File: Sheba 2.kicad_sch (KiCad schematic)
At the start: 66 parts, among them J2 Conn_01x03_Pin, J3 Conn_01x03_Pin, J4 Conn_01x03_Pin, J7 Conn_01x06_Pin, J8 Conn_01x02_Pin, J9 Conn_02x04_Top_Bottom, P1 USB_C_Plug_USB2.0, SW1 SW_SPDT, U1 AP62300TWU, U3 MIC5504-3.3YM5, U4 STM32F072CBTx

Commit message: Actually get ready to add protections
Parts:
- removed Battery1: XT-60, Connector_AMASS:AMASS_XT60-F_1x02_P7.20mm_Vertical, symbol Device:Battery
- removed C1, C15: C0.1uF, Capacitor_SMD:C_1206_3216Metric_Pad1.33x1.80mm_HandSolder, symbol Device:C_Small
- removed C10, C12, C16, C18, C3, C5, C6, C7: C1uF, Capacitor_SMD:C_1206_3216Metric_Pad1.33x1.80mm_HandSolder, symbol Device:C_Small
- removed C11: C2.2uF, Capacitor_SMD:C_1206_3216Metric_Pad1.33x1.80mm_HandSolder, symbol Device:C_Small
- removed C13, C19: C22uF, Capacitor_SMD:C_1206_3216Metric_Pad1.33x1.80mm_HandSolder, symbol Device:C_Small
- removed C8: C10uF, Capacitor_SMD:C_1206_3216Metric_Pad1.33x1.80mm_HandSolder, symbol Device:C_Small
- removed C9: C0.01uF, Capacitor_SMD:C_1206_3216Metric_Pad1.33x1.80mm_HandSolder, symbol Device:C_Small
- removed D2, D4, D6, D7, D8: LED Green, LED_SMD:LED_1206_3216Metric_Pad1.42x1.75mm_HandSolder, symbol Device:LED
- removed D3, D5: LED Red, LED_SMD:LED_1206_3216Metric_Pad1.42x1.75mm_HandSolder, symbol Device:LED
- removed H1, H2, H3, H4: MountingHole_Pad, MountingHole:MountingHole_2.2mm_M2_DIN965_Pad, symbol Mechanical:MountingHole_Pad
- removed J2, J3, J4: Conn_01x03_Pin, Connector_PinSocket_2.54mm:PinSocket_1x03_P2.54mm_Vertical, symbol Connector:Conn_01x03_Pin
- removed L1: L3.3uH, Inductor_SMD:L_1206_3216Metric, symbol Device:L
- removed MD1, MD2, MD3: ZXBM5210-S, Package_SO:SOIC-8_3.9x4.9mm_P1.27mm, symbol Driver_Motor:ZXBM5210-S
- removed MT1: ICM-42670-P, Library:XDCR_ICM-42670-P, symbol ICM-42670-P:ICM-42670-P
- removed Motor Terminal1: 6x Motor Port, TerminalBlock_4Ucon:TerminalBlock_4Ucon_1x06_P3.50mm_Horizontal, symbol Connector:Screw_Terminal_01x06
- removed R10, R11, R12, R13, R6, R7, R8, R9: R220, Resistor_SMD:R_1206_3216Metric_Pad1.30x1.75mm_HandSolder, symbol Device:R
- removed R2, R4, R5: R10k, Resistor_SMD:R_1206_3216Metric_Pad1.30x1.75mm_HandSolder, symbol Device:R
- removed U1: AP62300TWU, Package_TO_SOT_SMD:TSOT-23-6_HandSoldering, symbol Regulator_Switching:AP62300TWU
- removed U3: MIC5504-3.3YM5, Package_TO_SOT_SMD:SOT-23-5_HandSoldering, symbol Regulator_Linear:MIC5504-3.3YM5
- D1: value LED Red -> LED Green; DigiKey 150120RS75000 -> 150120VS75000
- J1: renamed from J8; footprint Connector_PinHeader_2.54mm:PinHeader_1x02_P2.54mm_Vertical -> Connector_PinHeader_2.54mm:PinHeader_1x03_P2.54mm_Vertical; symbol Connector:Conn_01x02_Pin -> Connector:Conn_01x03_Pin
- R3: value R56.2k -> R220; DigiKey CRCW120652K3FKEA -> RMCF1206JT220R
- renumbered C2 to C1, C4 to C2, C14 to C3, C17 to C4, EP3 to EP1, EP1 to EP2, EP2 to EP3, J9 to J2, J7 to J3, R14 to R1, R1 to R2, U4 to U1
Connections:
- net +5V: no longer R3.1
- net BLINKY: now also R3.1
- net GND: now also D1.1 (K), J1.1 (Pin_1)
- net M3_REV: no longer D1.2 (A)
- net USART3_TX: now also J1.3 (Pin_3); no longer J1.1 (Pin_1)
- net at R3.2: now also D1.2 (A)
- net I2C2_SCL: no longer names the net of U1.26 (PB13)
- net I2C2_SDA: no longer names the net of U1.27 (PB14)
- net IMU_INT: no longer names the net of U1.28 (PB15)
- no-connect marks 12 -> 9
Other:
- added sheet Power & Motors (Power & Motors.kicad_sch)
- note added: "CPU STATUS LED"
- note added: "Kiwi/Differential Drive Switch"
- note removed: "12V to 5V"
- note removed: "3V3 LDO Power Supply"
- note removed: "AP_CS wired to VDD for I2C mode"
- note removed: "I2C Pull-ups"
- note removed: "IMU - Accel/Gyro/Temp chip ICM-42670-P"
- note removed: "Indicator LEDs"
- note removed: "Motor Controllers"
- note removed: "Servo Ports"
- note removed: "VIN: 4.2 to 18V"
- note removed: "VREF is wired to VDD to enable PWM control"
- moved on the sheet: C1, C2, C3, C4, EP1, EP2, EP3, J2, J3, P1, R1, R2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

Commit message: Ready to finalize Rev3
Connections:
- net GPIO0: now also U1.4 (PC15); no longer U1.42 (PB6)
- net GPIO5: now also U1.42 (PB6); no longer U1.4 (PC15)

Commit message: Rev3 ready to order
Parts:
- P1: value USB_C_Plug_USB2.0 -> USB 2.0 Type-C Port
- SW1: value SW_SPDT -> SPDT Switch
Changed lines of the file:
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@@
 			)
 		)
-		(property "Value" "USB_C_Plug_USB2.0"
+		(property "Value" "USB 2.0 Type-C Port"
 			(at 161.29 71.12 0)
 			(effects
@@
 			)
 		)
-		(property "Value" "SW_SPDT"
+		(property "Value" "SPDT Switch"
 			(at 105.41 95.25 0)
 			(effects

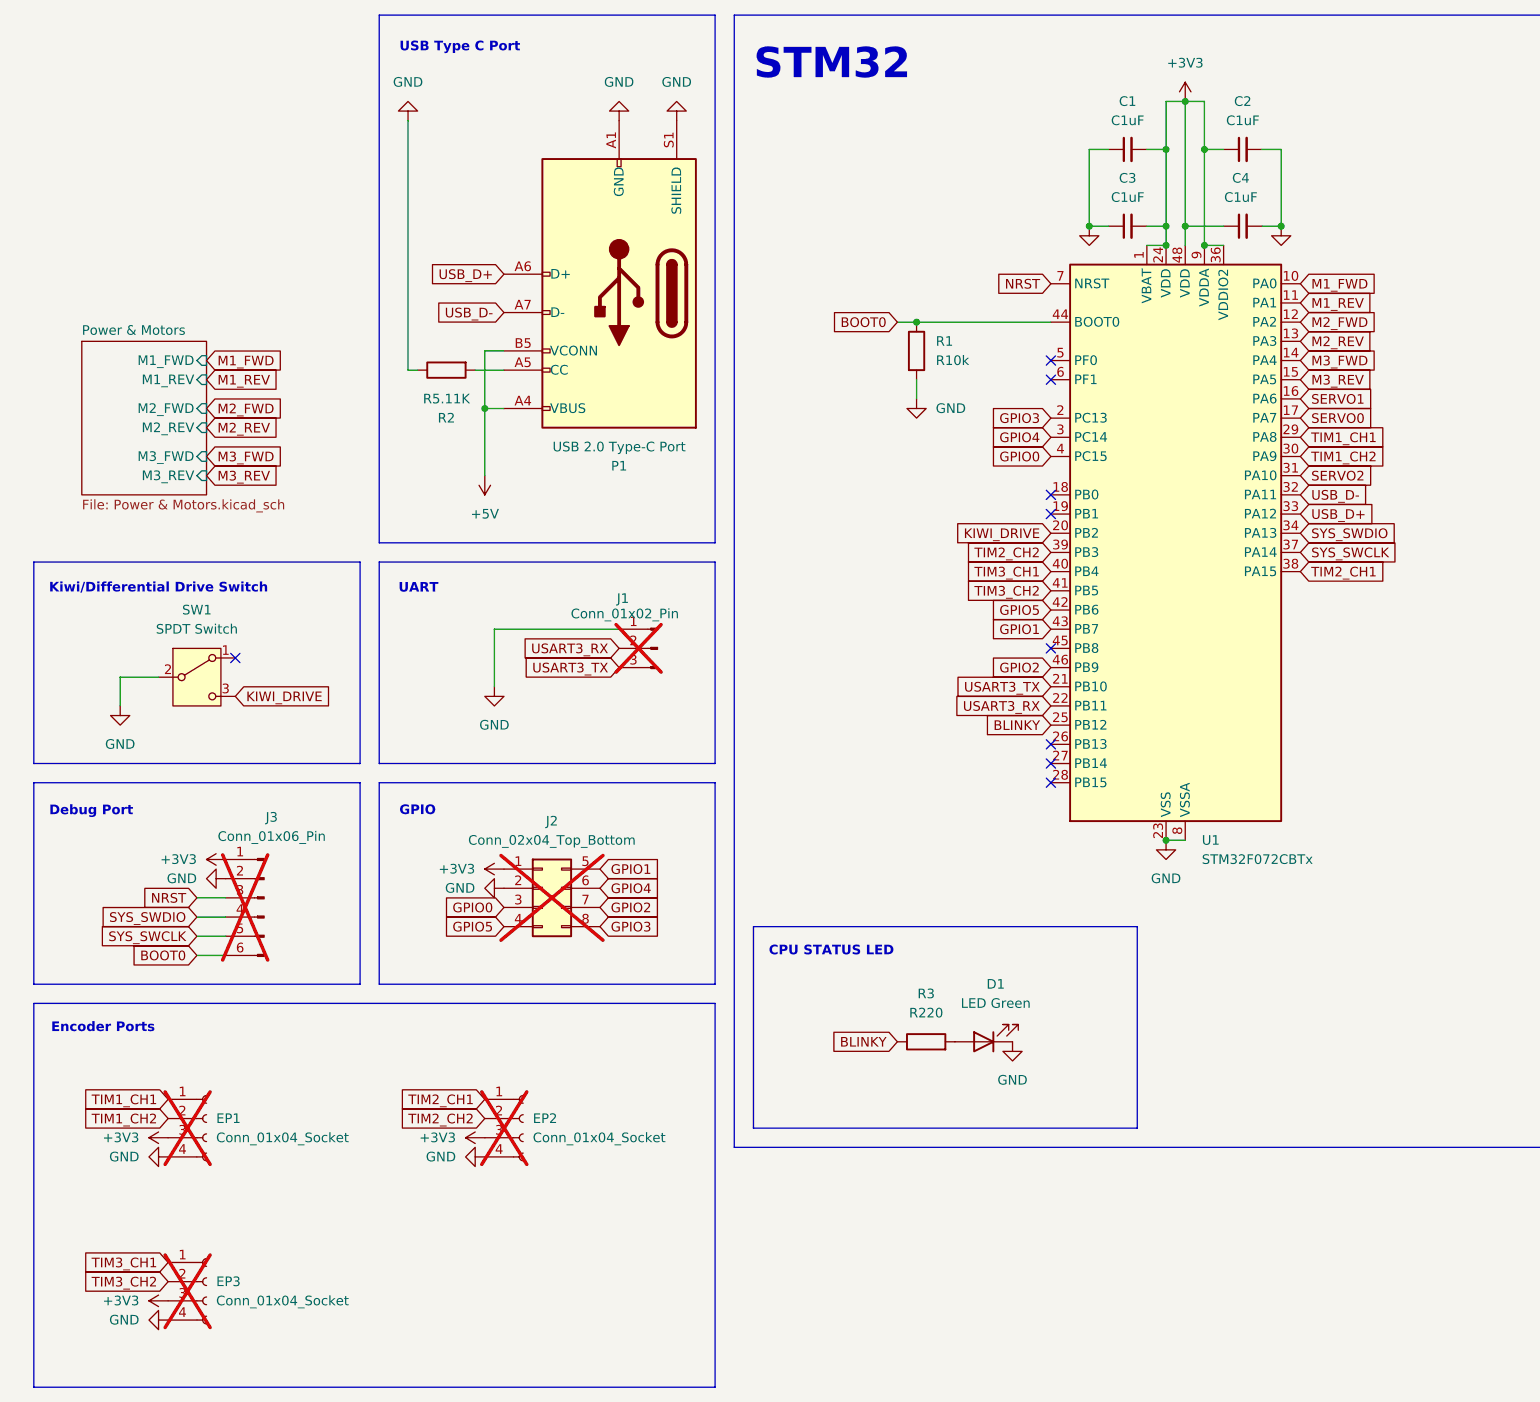
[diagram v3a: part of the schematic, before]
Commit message: Rewire the entire thing to use hardware PWM and software quadrature decoding
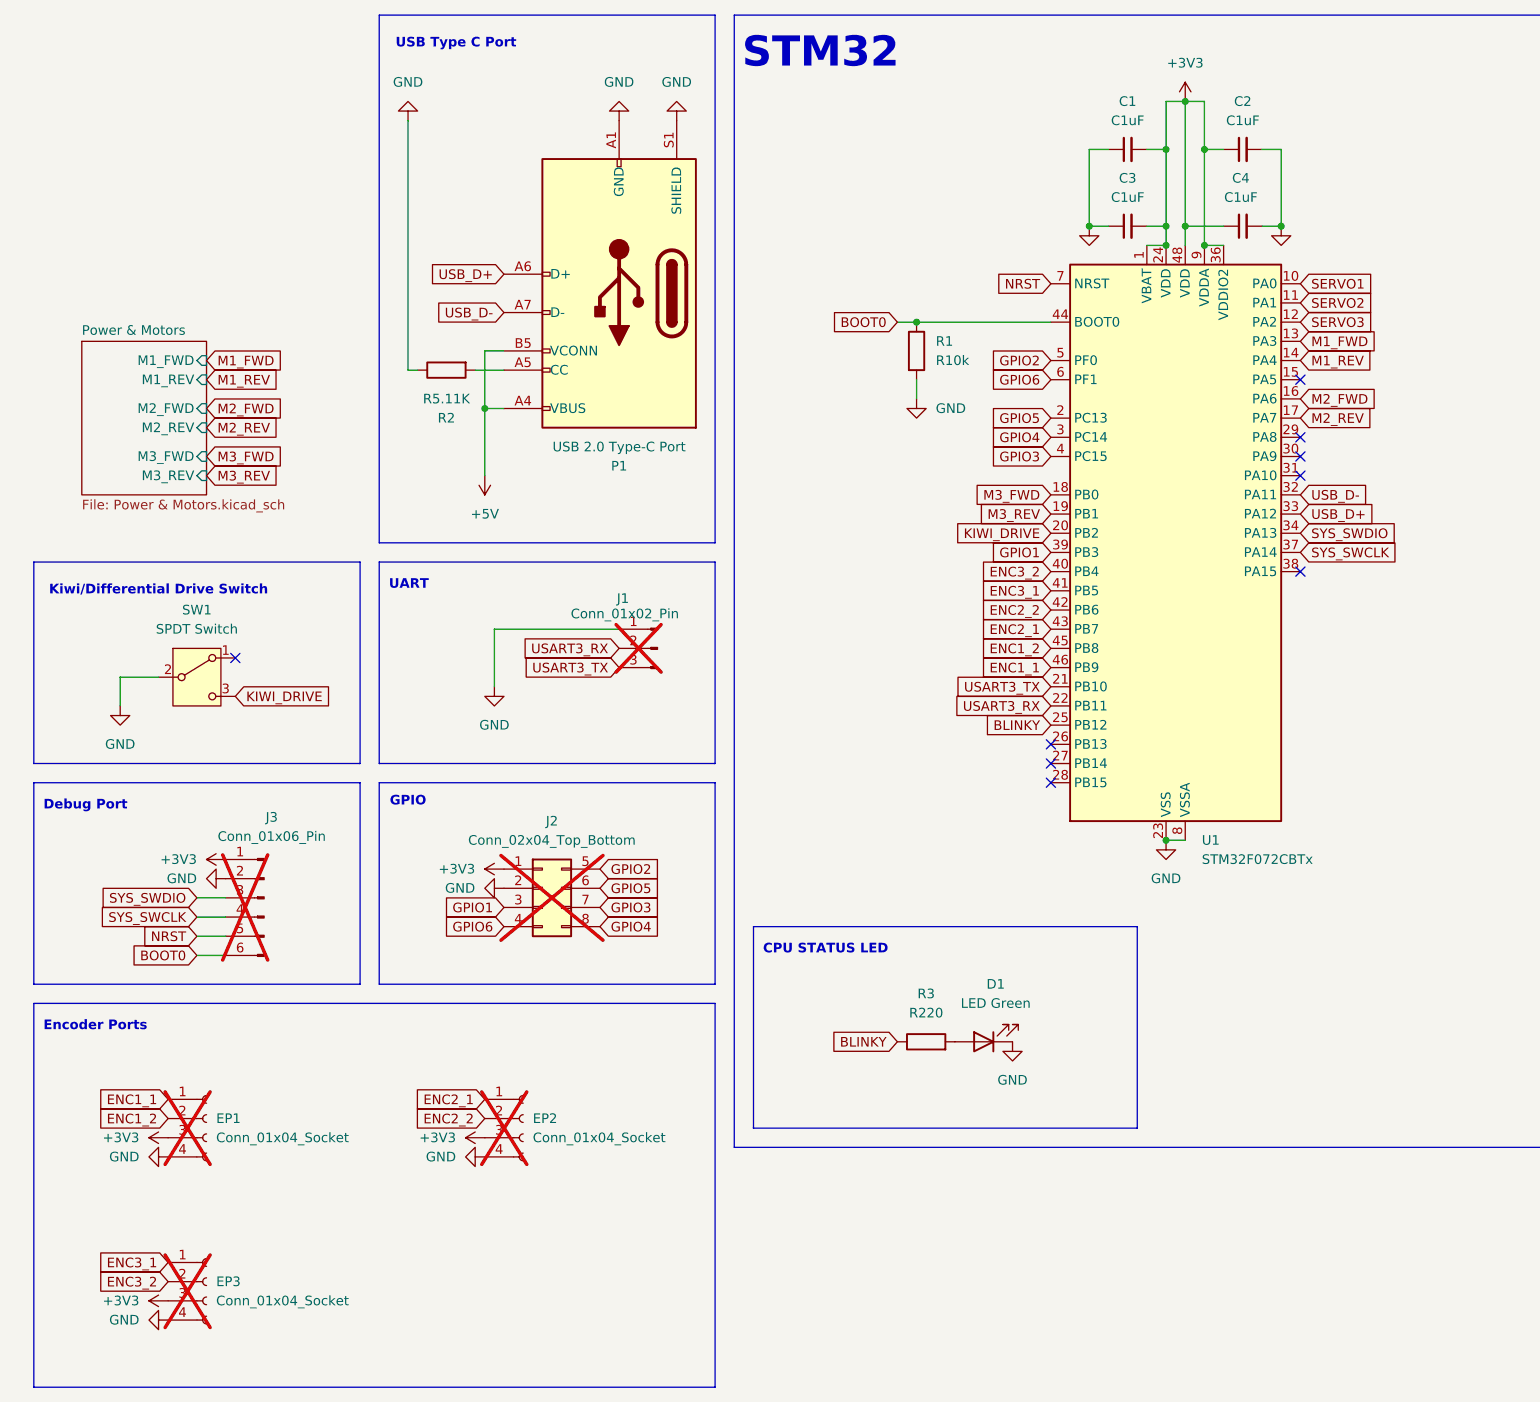
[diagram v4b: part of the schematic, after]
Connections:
- net SERVO0 is gone; now on net M2_REV: U1.17 (PA7)
- net GPIO1: now also J2.3 (Pin_3), U1.39 (PB3); no longer J2.5 (Pin_5), U1.43 (PB7)
- net GPIO2: now also J2.5 (Pin_5), U1.5 (PF0); no longer J2.7 (Pin_7), U1.46 (PB9)
- net GPIO3: now also J2.7 (Pin_7), U1.4 (PC15); no longer J2.8 (Pin_8), U1.2 (PC13)
- net GPIO4: now also J2.8 (Pin_8); no longer J2.6 (Pin_6)
- net GPIO5: now also J2.6 (Pin_6), U1.2 (PC13); no longer J2.4 (Pin_4), U1.42 (PB6)
- net M1_FWD: now also U1.13 (PA3); no longer U1.10 (PA0)
- net M1_REV: now also U1.14 (PA4); no longer U1.11 (PA1)
- net M2_FWD: now also U1.16 (PA6); no longer U1.12 (PA2)
- net M2_REV: no longer U1.13 (PA3)
- net M3_FWD: now also U1.18 (PB0); no longer U1.14 (PA4)
- net M3_REV: now also U1.19 (PB1); no longer U1.15 (PA5)
- net NRST: now also J3.5 (Pin_5); no longer J3.3 (Pin_3)
- net SERVO1: now also U1.10 (PA0); no longer U1.16 (PA6)
- net SERVO2: now also U1.11 (PA1); no longer U1.31 (PA10)
- net SYS_SWCLK: now also J3.4 (Pin_4); no longer J3.5 (Pin_5)
- net SYS_SWDIO: now also J3.3 (Pin_3); no longer J3.4 (Pin_4)
- net ENC1_2: now reaches U1.45 (PB8)
- net ENC1_2: now also EP1.2 (Pin_2)
- net GPIO6: now reaches U1.6 (PF1)
- net GPIO6: now also J2.4 (Pin_4)
- removed net GPIO0: J2.3 (Pin_3), U1.4 (PC15)
- net TIM1_CH1: no longer names the net of U1.29 (PA8)
- net TIM1_CH1: no longer EP1.1 (Pin_1)
- net TIM1_CH2: no longer names the net of U1.30 (PA9)
- net TIM1_CH2: no longer EP1.2 (Pin_2)
- net TIM2_CH1: no longer names the net of U1.38 (PA15)
- net TIM2_CH1: no longer EP2.1 (Pin_1)
- net TIM2_CH2 renamed ENC2_2
- net ENC2_2: now also U1.42 (PB6); no longer U1.39 (PB3)
- net TIM3_CH1 renamed ENC3_1
- net ENC3_1: now also U1.41 (PB5); no longer U1.40 (PB4)
- net TIM3_CH2 renamed ENC3_2
- net ENC3_2: now also U1.40 (PB4); no longer U1.41 (PB5)
- new net ENC1_1: EP1.1 (Pin_1), U1.46 (PB9)
- new net ENC2_1: EP2.1 (Pin_1), U1.43 (PB7)
- new net SERVO3: U1.12 (PA2)
